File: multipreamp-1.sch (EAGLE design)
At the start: 140 parts, among them Q1 J201, Q2 J201, Q3 J201, Q4 J201, Q5 J201, Q6 J201, Q7 J201, Q8 2N5088

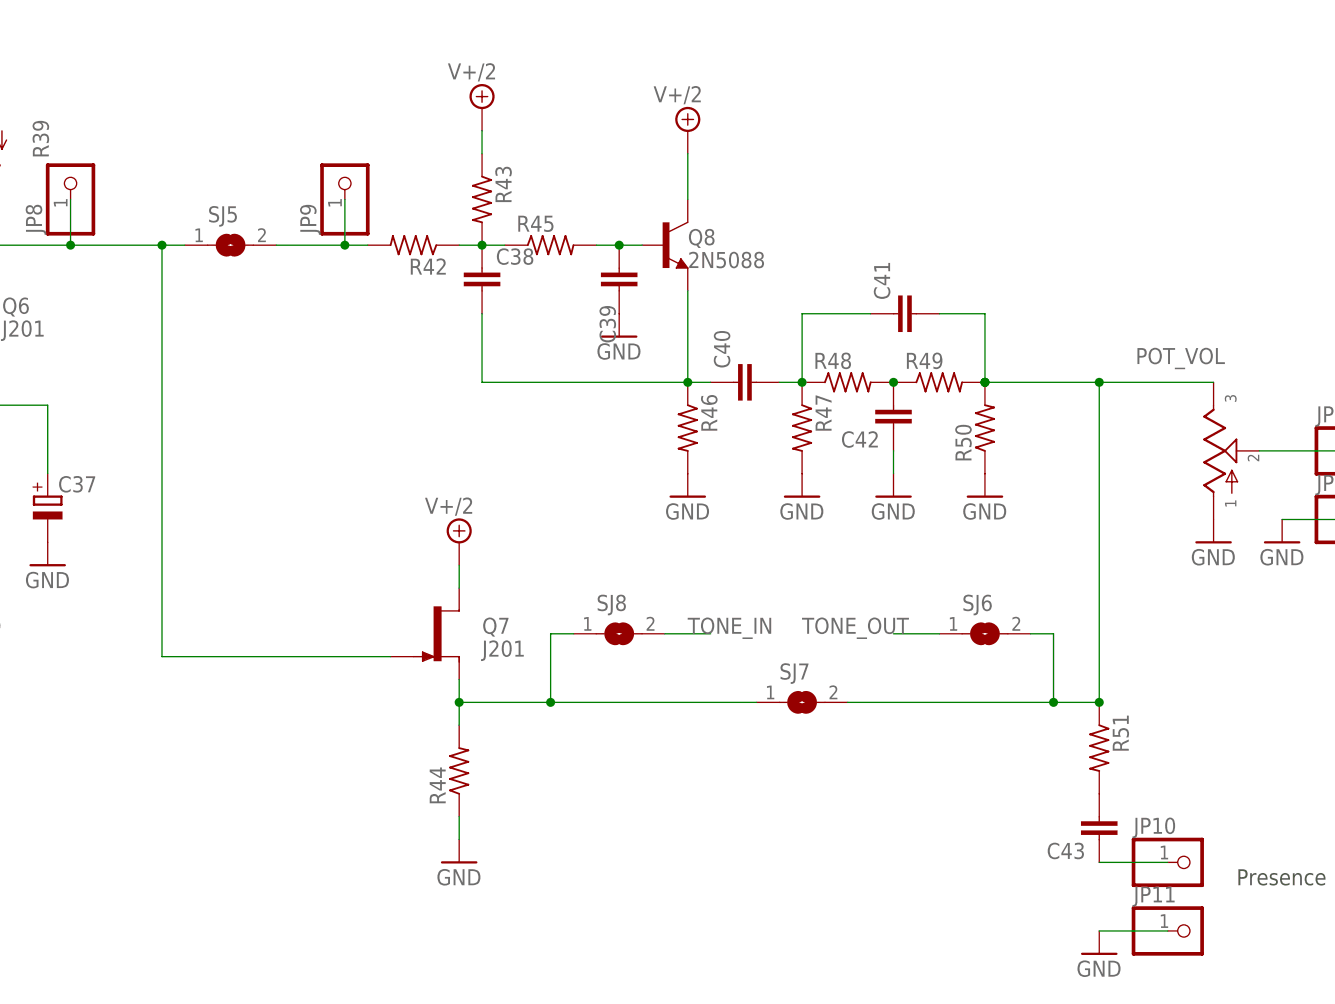
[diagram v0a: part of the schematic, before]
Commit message: Ajustes no esquematico e layout - Adicao de capacitor em serie com buffer FET de saida, ajuste de posicionamento de labels, adicao de vias
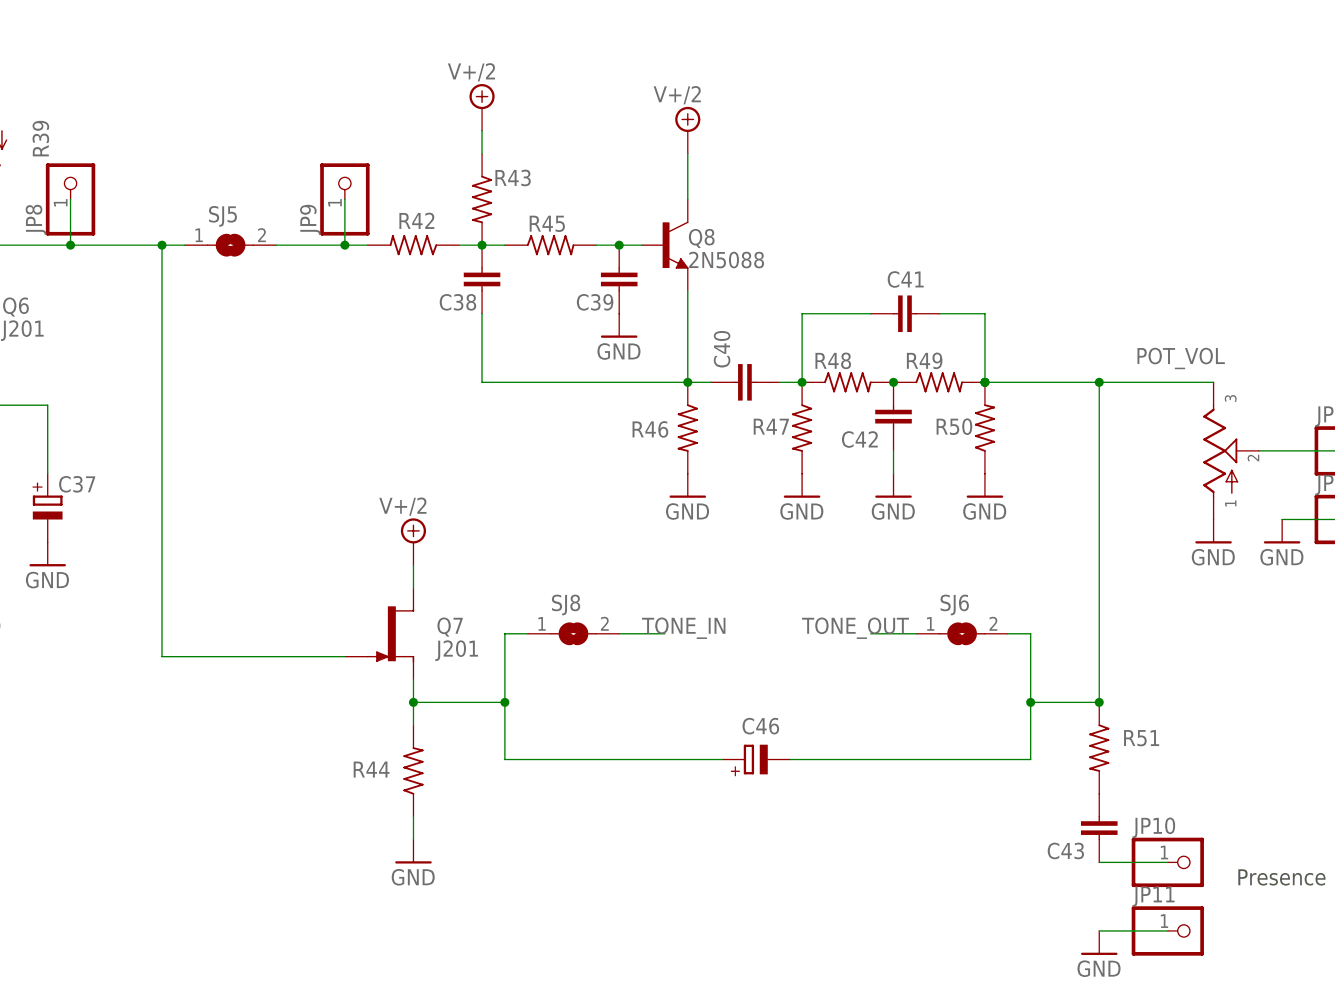
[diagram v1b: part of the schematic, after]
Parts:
- removed SJ7: (no value), jumper:SJ
- added C46: (no value), rcl:CPOL-EUE2.5-6
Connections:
- net N$45: now also C46.+; no longer SJ7.1
- net N$9: now also C46.-; no longer SJ7.2
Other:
- moved on the sheet: Q7, R44, SJ6, SJ8

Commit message: Ajustes finais no layout e esquematico - posicionamento de labels, troca de testpoints por pinheads, adicao de assinatura na placa Gerber v1.0 gerado com base nessa versao
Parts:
- removed TP1, TP2: PTR1PAD1-13, testpad:PTR1PAD1-13
- added JP14: P1, pinhead:PINHD-1X1
- added JP15: P3, pinhead:PINHD-1X1
- JP1: value (none) -> V+
- JP10: value (none) -> PRES
- JP11, JP13, JP2, JP4, JP6: value (none) -> GND
- JP12: value (none) -> OUT
- JP3: value (none) -> IN
- JP5: value (none) -> SW
- JP7: value (none) -> P2
- JP8: value (none) -> P4
- JP9: value (none) -> P5
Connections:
- net N$22: now also JP15.1; no longer TP2.TP
- net N$8: now also JP14.1; no longer TP1.TP
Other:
- note removed: "Ponto para chave Clean/Dirt Azabache"
- moved on the sheet: C29, JP11, JP13, JP4, JP7, JP8, JP9, R27, R33
